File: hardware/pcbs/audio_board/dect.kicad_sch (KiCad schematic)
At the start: 1 part, among them J10 DECT

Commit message: fix libraries
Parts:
- J9: renamed from J10; footprint Library:DectModule -> extra:DectModule
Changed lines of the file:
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@@
 		(dnp no)
 		(fields_autoplaced yes)
-		(property "Reference" "#PWR034"
+		(property "Reference" "#PWR0112"
 			(at 146.05 95.25 0)
 			(effects
@@
 			(project "audio_board"
 				(path "/54443f96-c7c5-4432-b890-45b14a1547a1/c4fe3322-408e-4a63-9af2-adca55ba4923"
-					(reference "#PWR034")
+					(reference "#PWR0112")
 					(unit 1)
 				)
@@
 		(dnp no)
 		(fields_autoplaced yes)
-		(property "Reference" "J10"
+		(property "Reference" "J9"
 			(at 154.94 87.63 0)
 			(effects
@@
 			)
 		)
-		(property "Footprint" "Library:DectModule"
+		(property "Footprint" "extra:DectModule"
 			(at 153.67 99.06 0)
 			(effects
@@
 			(project "audio_board"
 				(path "/54443f96-c7c5-4432-b890-45b14a1547a1/c4fe3322-408e-4a63-9af2-adca55ba4923"
-					(reference "J10")
+					(reference "J9")
 					(unit 1)
 				)
@@
 		(dnp no)
 		(fields_autoplaced yes)
-		(property "Reference" "#PWR033"
+		(property "Reference" "#PWR0113"
 			(at 146.05 114.3 0)
 			(effects
@@
 			(project "audio_board"
 				(path "/54443f96-c7c5-4432-b890-45b14a1547a1/c4fe3322-408e-4a63-9af2-adca55ba4923"
-					(reference "#PWR033")
+					(reference "#PWR0113")
 					(unit 1)
 				)

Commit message: routing almost complete
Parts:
- removed J9: DECT, extra:DectModule, symbol Connector_Generic:Conn_02x06_Top_Bottom
- added J9: Conn_01x12, Connector_PinHeader_2.54mm:PinHeader_1x12_P2.54mm_Vertical, symbol Connector_Generic:Conn_01x12
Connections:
- net +5V: now also J9.1 (Pin_1)
- net GND: now also J9.12 (Pin_12)
- net INT: now also J9.8 (Pin_8)
- net RESET: now also J9.9 (Pin_9)
- net RX: now also J9.11 (Pin_11)
- net SCL: now also J9.6 (Pin_6)
- net SDA: now also J9.7 (Pin_7)
- net TDM_FSYNC: now also J9.3 (Pin_3)
- net TDM_RX: now also J9.2 (Pin_2)
- net TDM_SCLK: now also J9.4 (Pin_4)
- net TDM_TX: now also J9.5 (Pin_5)
- net TX: now also J9.10 (Pin_10)

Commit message: component values
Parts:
- J9: MPN (none) -> Header_1x12
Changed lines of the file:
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@@
+			)
+		)
+		(property "MPN" "Header_1x12"
+			(at 153.67 106.68 0)
+			(effects
+				(font
+					(size 1.27 1.27)
+				)
+				(hide yes)
 			)
 		)

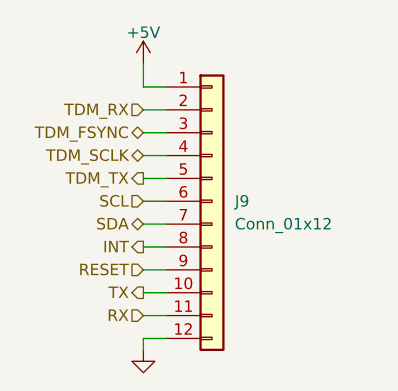
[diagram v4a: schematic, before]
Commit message: finish silkscreens
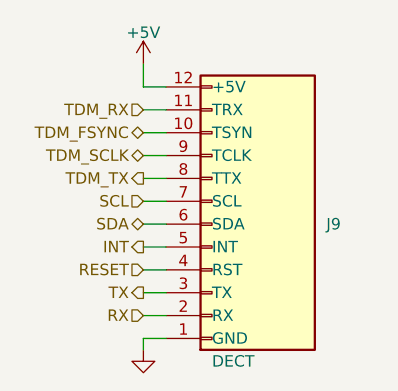
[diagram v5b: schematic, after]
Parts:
- removed J9: Conn_01x12, Connector_PinHeader_2.54mm:PinHeader_1x12_P2.54mm_Vertical, symbol Connector_Generic:Conn_01x12
- added J9: Header_01x12, conn:PinHeader_1x12_P2.54mm_Vertical_1, symbol conn:Conn_01x12
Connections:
- net +5V: now also J9.12 (Pin_12)
- net GND: now also J9.1 (Pin_1)
- net INT: now also J9.5 (Pin_5)
- net RESET: now also J9.4 (Pin_4)
- net RX: now also J9.2 (Pin_2)
- net SCL: now also J9.7 (Pin_7)
- net SDA: now also J9.6 (Pin_6)
- net TDM_FSYNC: now also J9.10 (Pin_10)
- net TDM_RX: now also J9.11 (Pin_11)
- net TDM_SCLK: now also J9.9 (Pin_9)
- net TDM_TX: now also J9.8 (Pin_8)
- net TX: now also J9.3 (Pin_3)
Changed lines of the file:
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@@
+	)
+	(symbol
+		(lib_id "conn:Conn_01x12")
+		(at 153.67 119.38 0)
+		(mirror x)
+		(unit 1)
+		(exclude_from_sim no)
+		(in_bom yes)
+		(on_board yes)
+		(dnp no)
+		(property "Reference" "J9"
+			(at 166.37 109.2201 0)
+			(effects
+				(font
+					(size 1.27 1.27)
+				)
+				(justify left)
+			)
+		)
+		(property "Value" "Header_01x12"
+			(at 157.988 91.694 0)
+			(effects
+				(font
+					(size 1.27 1.27)
+				)
+				(hide yes)
+			)
+		)
+		(property "Footprint" "conn:PinHeader_1x12_P2.54mm_Vertical_1"
+			(at 153.67 123.698 0)
+			(effects
+				(font
+					(size 1.27 1.27)
+				)
+				(hide yes)
+			)
+		)
+		(property "Datasheet" "~"
+			(at 153.67 119.38 0)
+			(effects
+				(font
+					(size 1.27 1.27)
+				)
+				(hide yes)
+			)
+		)
+		(property "Description" "Generic connector, single row, 01x06, script generated (kicad-library-utils/schlib/autogen/connector/)"
+			(at 153.924 123.698 0)
+			(effects
+				(font
+					(size 1.27 1.27)
+				)
+				(hide yes)
+			)
+		)
+		(property "Purpose Pin1" "GND"
+			(at 153.67 121.92 0)
+			(do_not_autoplace yes)
+			(effects
+				(font
+					(size 1.27 1.27)
+				)
+				(justify left)
+			)
+		)
+		(property "Purpose Pin2" "RX"
+			(at 153.67 119.38 0)
+			(do_not_autoplace yes)
+			(effects
+				(font
+					(size 1.27 1.27)
+				)
+				(justify left)
+			)
+		)
+		(property "Purpose Pin3" "TX"
+			(at 153.67 116.84 0)
+			(do_not_autoplace yes)
+			(effects
+				(font
+					(size 1.27 1.27)
+				)
+				(justify left)
+			)
+		)
+		(property "Purpose Pin4" "RST"
+			(at 153.67 114.3 0)
+			(do_not_autoplace yes)
+			(effects
+				(font
+					(size 1.27 1.27)
+				)
+				(justify left)
+			)
+		)
+		(property "Purpose Pin5" "INT"
+			(at 153.67 111.76 0)
+			(do_not_autoplace yes)
+			(effects
+				(font
+					(size 1.27 1.27)
+				)
+				(justify left)
+			)
+		)
+		(property "Purpose Pin6" "SDA"
+			(at 153.67 109.22 0)
+			(do_not_autoplace yes)
+			(effects
+				(font
+					(size 1.27 1.27)
+				)
+				(justify left)
+			)
+		)
+		(property "Purpose Pin7" "SCL"
+			(at 153.67 106.68 0)
+			(do_not_autoplace yes)
+			(effects
+				(font
+					(size 1.27 1.27)
+				)
+				(justify left)
+			)
+		)
+		(property "Purpose Pin8" "TTX"
+			(at 153.67 104.14 0)
+			(do_not_autoplace yes)
+			(effects
+				(font
+					(size 1.27 1.27)
+				)
+				(justify left)
+			)
+		)
+		(property "Purpose Pin9" "TCLK"
+			(at 153.67 101.6 0)
+			(do_not_autoplace yes)
+			(effects
+				(font
+					(size 1.27 1.27)
+				)
+				(justify left)
+			)
+		)
+		(property "Purpose Pin10" "TSYN"
+			(at 153.67 99.06 0)
+			(do_not_autoplace yes)
+			(effects
+				(font
+					(size 1.27 1.27)
+				)
+				(justify left)
+			)
+		)
+		(property "Purpose Pin11" "TRX"
+			(at 153.67 96.52 0)
+			(do_not_autoplace yes)
+			(effects
+				(font
+					(size 1.27 1.27)
+				)
+				(justify left)
+			)
+		)
+		(property "Purpose Pin12" "+5V"
+			(at 153.67 93.98 0)
+			(do_not_autoplace yes)
+			(effects
+				(font
+					(size 1.27 1.27)
+				)
+				(justify left)
+			)
+		)
+		(property "Purpose" "DECT"
+			(at 153.67 124.46 0)
+			(effects
+				(font
+					(size 1.27 1.27)
+				)
+				(justify left)
+			)
+		)
+		(pin "12"
+		)
+		(pin "11"
+		)
+		(pin "2"
+		)
+		(pin "1"
+		)
+		(pin "9"
+		)
+		(pin "10"
+		)
+		(pin "3"
+		)
+		(pin "4"
+		)
+		(pin "6"
+		)
+		(pin "7"
+		)
+		(pin "8"
+		)
+		(pin "5"
+		)
+		(instances
+			(project ""
+				(path "/54443f96-c7c5-4432-b890-45b14a1547a1/c4fe3322-408e-4a63-9af2-adca55ba4923"
+					(reference "J9")
+					(unit 1)
+				)
+			)
+		)
 	)
 	(symbol
@@
 					(unit 1)
 				)
-			)
-		)
-	)
-	(symbol
-		(lib_id "Connector_Generic:Conn_01x12")
-		(at 153.67 106.68 0)
-		(unit 1)
-		(exclude_from_sim no)
-		(in_bom yes)
-		(on_board yes)
-		(dnp no)
-		(fields_autoplaced yes)
-		(property "Reference" "J9"
-			(at 156.21 106.6799 0)
-			(effects
-				(font
-					(size 1.27 1.27)
-				)
-				(justify left)
-			)
-		)
-		(property "Value" "Conn_01x12"
-			(at 156.21 109.2199 0)
-			(effects
-				(font
-					(size 1.27 1.27)
-				)
-				(justify left)
-			)
-		)
-		(property "Footprint" "Connector_PinHeader_2.54mm:PinHeader_1x12_P2.54mm_Vertical"
-			(at 153.67 106.68 0)
-			(effects
-				(font
-					(size 1.27 1.27)
-				)
-				(hide yes)
-			)
-		)
-		(property "Datasheet" "~"
-			(at 153.67 106.68 0)
-			(effects
-				(font
-					(size 1.27 1.27)
-				)
-				(hide yes)
-			)
-		)
-		(property "Description" "Generic connector, single row, 01x12, script generated (kicad-library-utils/schlib/autogen/connector/)"
-			(at 153.67 106.68 0)
-			(effects
-				(font
-					(size 1.27 1.27)
-				)
-				(hide yes)
-			)
-		)
-		(property "MPN" "Header_1x12"
-			(at 153.67 106.68 0)
-			(effects
-				(font
-					(size 1.27 1.27)
-				)
-				(hide yes)
-			)
-		)
-		(pin "6"
-		)
-		(pin "11"
-		)
-		(pin "9"
-		)
-		(pin "12"
-		)
-		(pin "10"
-		)
-		(pin "2"
-		)
-		(pin "3"
-		)
-		(pin "4"
-		)
-		(pin "8"
-		)
-		(pin "1"
-		)
-		(pin "5"
-		)
-		(pin "7"
-		)
-		(instances
-			(project ""
-				(path "/54443f96-c7c5-4432-b890-45b14a1547a1/c4fe3322-408e-4a63-9af2-adca55ba4923"
-					(reference "J9")
-					(unit 1)
-				)

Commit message: final touches before production
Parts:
- J9: MPN (none) -> PinHeader_01x12
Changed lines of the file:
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@@
+			)
+		)
+		(property "MPN" "PinHeader_01x12"
+			(at 153.67 119.38 0)
+			(effects
+				(font
+					(size 1.27 1.27)
+				)
+				(hide yes)
 			)
 		)
